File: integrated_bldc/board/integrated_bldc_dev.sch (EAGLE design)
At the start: 107 parts, among them J2 PRG

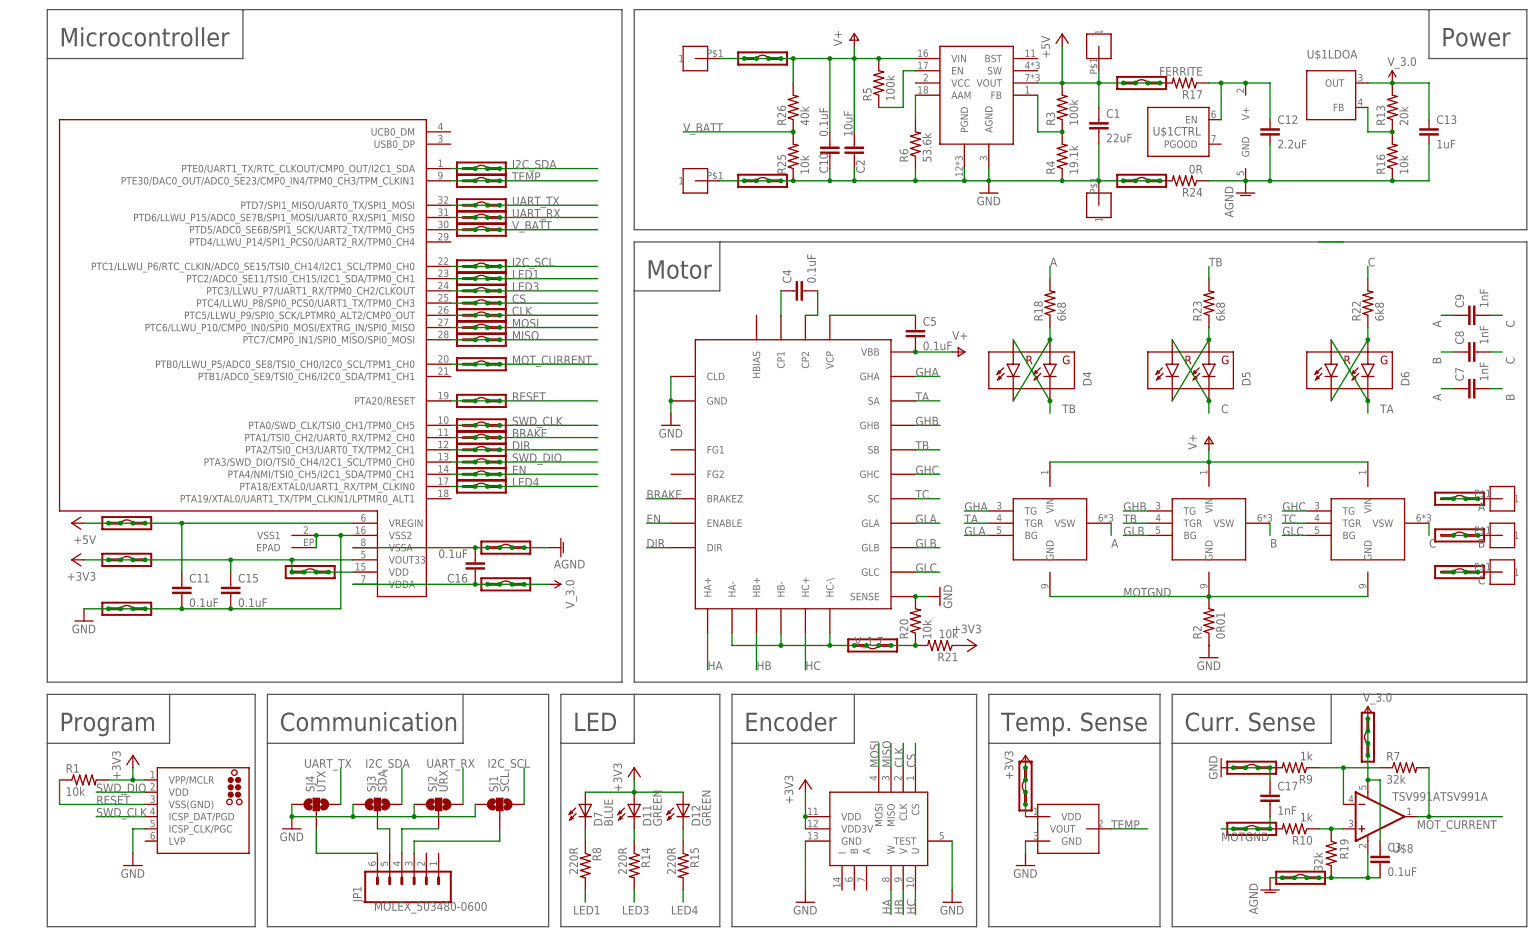
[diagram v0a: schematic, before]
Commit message: Finished Dev board layout. Added stop mask to vias. Corrected some component values based on part order.
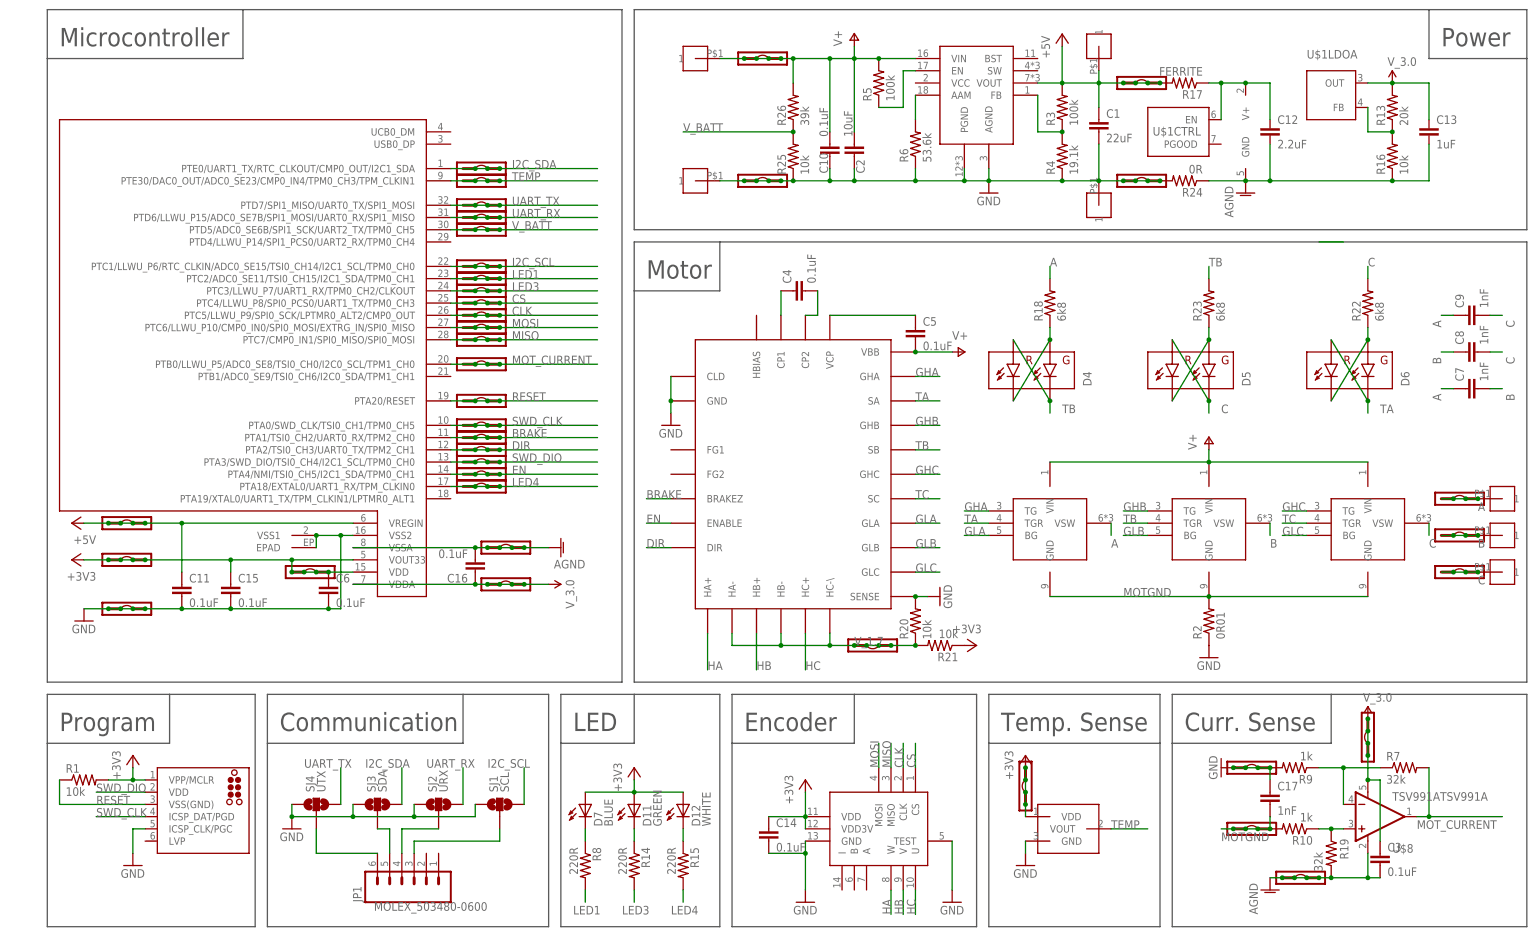
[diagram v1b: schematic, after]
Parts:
- added C14, C6: 0.1uF, SparkFun-Passives:CAP0402-CAP
- D12: value GREEN -> WHITE
- R26: value 40k -> 39k
- renumbered MOTA to A, MOTB to B, MOTC to C
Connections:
- net +3V3: now also C14.1, C6.1
- net GND: now also C14.2, C6.2
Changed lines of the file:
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@@
 <part name="D7" library="SparkFun-LED" deviceset="LED-BLUE" device="0603" value="BLUE"/>
 <part name="D11" library="SparkFun-LED" deviceset="LED-GREEN" device="0603" value="GREEN"/>
-<part name="D12" library="SparkFun-LED" deviceset="LED-GREEN" device="0603" value="GREEN"/>
+<part name="D12" library="SparkFun-LED" deviceset="LED-GREEN" device="0603" value="WHITE"/>
 <part name="R8" library="SparkFun-Passives" deviceset="RESISTOR" device="0402-RES" value="220R"/>
 <part name="R14" library="SparkFun-Passives" deviceset="RESISTOR" device="0402-RES" value="220R"/>
@@
 <part name="P+4" library="supply1" deviceset="V+" device=""/>
 <part name="R25" library="biomimetic" deviceset="RESISTOR" device="0402-RES" value="10k"/>
-<part name="R26" library="biomimetic" deviceset="RESISTOR" device="0402-RES" value="40k"/>
+<part name="R26" library="biomimetic" deviceset="RESISTOR" device="0402-RES" value="39k"/>
 <part name="P+5" library="supply1" deviceset="V+" device=""/>
 <part name="+3V4" library="supply1" deviceset="+3V3" device=""/>
@@
 <part name="V3.0" library="modular_robotics" deviceset="M04" device="LOCK"/>
 <part name="V1.7" library="modular_robotics" deviceset="M04" device="LOCK"/>
-<part name="MOTA" library="modular_robotics" deviceset="M04" device="LOCK"/>
-<part name="MOTB" library="modular_robotics" deviceset="M04" device="LOCK"/>
-<part name="MOTC" library="modular_robotics" deviceset="M04" device="LOCK"/>
+<part name="A" library="modular_robotics" deviceset="M04" device="LOCK"/>
+<part name="B" library="modular_robotics" deviceset="M04" device="LOCK"/>
+<part name="C" library="modular_robotics" deviceset="M04" device="LOCK"/>
+<part name="C6" library="SparkFun-Passives" deviceset="CAP" device="0402-CAP" value="0.1uF"/>
+<part name="C14" library="SparkFun-Passives" deviceset="CAP" device="0402-CAP" value="0.1uF"/>
 </parts>
 <sheets>
@@
 <instance part="V3.0" gate="G$1" x="208.28" y="119.38" rot="R180"/>
 <instance part="V1.7" gate="G$1" x="104.14" y="137.16" rot="R270"/>
-<instance part="MOTA" gate="G$1" x="228.6" y="167.64" rot="R90"/>
-<instance part="MOTB" gate="G$1" x="228.6" y="160.02" rot="R90"/>
-<instance part="MOTC" gate="G$1" x="228.6" y="152.4" rot="R90"/>
+<instance part="A" gate="G$1" x="228.6" y="167.64" rot="R90"/>
+<instance part="B" gate="G$1" x="228.6" y="160.02" rot="R90"/>
+<instance part="C" gate="G$1" x="228.6" y="152.4" rot="R90"/>
+<instance part="C6" gate="G$1" x="-7.62" y="147.32"/>
+<instance part="C14" gate="G$1" x="83.82" y="96.52"/>
 </instances>
 <busses>
@@
 <label x="231.14" y="165.1" size="1.778" layer="95"/>
 <pinref part="U$10" gate="G$1" pin="1"/>
-<pinref part="MOTA" gate="G$1" pin="1"/>
+<pinref part="A" gate="G$1" pin="1"/>
 <junction x="231.14" y="167.64"/>
-<pinref part="MOTA" gate="G$1" pin="2"/>
+<pinref part="A" gate="G$1" pin="2"/>
 <wire x1="228.6" y1="167.64" x2="226.06" y2="167.64" width="0.1524" layer="91"/>
 <junction x="228.6" y="167.64"/>
-<pinref part="MOTA" gate="G$1" pin="3"/>
+<pinref part="A" gate="G$1" pin="3"/>
 <wire x1="226.06" y1="167.64" x2="223.52" y2="167.64" width="0.1524" layer="91"/>
 <junction x="226.06" y="167.64"/>
-<pinref part="MOTA" gate="G$1" pin="4"/>
+<pinref part="A" gate="G$1" pin="4"/>
 </segment>
 <segment>
@@
 <label x="231.14" y="157.48" size="1.778" layer="95"/>
 <pinref part="U$11" gate="G$1" pin="1"/>
-<pinref part="MOTB" gate="G$1" pin="1"/>
+<pinref part="B" gate="G$1" pin="1"/>
 <junction x="231.14" y="160.02"/>
-<pinref part="MOTB" gate="G$1" pin="2"/>
+<pinref part="B" gate="G$1" pin="2"/>
 <wire x1="228.6" y1="160.02" x2="226.06" y2="160.02" width="0.1524" layer="91"/>
 <junction x="228.6" y="160.02"/>
-<pinref part="MOTB" gate="G$1" pin="3"/>
+<pinref part="B" gate="G$1" pin="3"/>
 <wire x1="226.06" y1="160.02" x2="223.52" y2="160.02" width="0.1524" layer="91"/>
 <junction x="226.06" y="160.02"/>
-<pinref part="MOTB" gate="G$1" pin="4"/>
+<pinref part="B" gate="G$1" pin="4"/>
 </segment>
 <segment>
@@
 <label x="231.14" y="149.86" size="1.778" layer="95"/>
 <pinref part="U$12" gate="G$1" pin="1"/>
-<pinref part="MOTC" gate="G$1" pin="1"/>
+<pinref part="C" gate="G$1" pin="1"/>
 <junction x="231.14" y="152.4"/>
-<pinref part="MOTC" gate="G$1" pin="2"/>
+<pinref part="C" gate="G$1" pin="2"/>
 <wire x1="228.6" y1="152.4" x2="226.06" y2="152.4" width="0.1524" layer="91"/>
 <junction x="228.6" y="152.4"/>
-<pinref part="MOTC" gate="G$1" pin="3"/>
+<pinref part="C" gate="G$1" pin="3"/>
 <wire x1="226.06" y1="152.4" x2="223.52" y2="152.4" width="0.1524" layer="91"/>
 <junction x="226.06" y="152.4"/>
-<pinref part="MOTC" gate="G$1" pin="4"/>
+<pinref part="C" gate="G$1" pin="4"/>
 </segment>
 <segment>
@@
 <pinref part="GND6" gate="1" pin="GND"/>
 <pinref part="AS5047P" gate="G$1" pin="GND"/>
-<wire x1="91.44" y1="86.36" x2="91.44" y2="96.52" width="0.1524" layer="91"/>
+<wire x1="91.44" y1="86.36" x2="91.44" y2="93.98" width="0.1524" layer="91"/>
+<pinref part="C14" gate="G$1" pin="2"/>
+<wire x1="91.44" y1="93.98" x2="91.44" y2="96.52" width="0.1524" layer="91"/>
+<wire x1="91.44" y1="93.98" x2="83.82" y2="93.98" width="0.1524" layer="91"/>
+<junction x="91.44" y="93.98"/>
 </segment>
 <segment>
@@
 <wire x1="-10.16" y1="157.48" x2="-10.16" y2="160.02" width="0.1524" layer="91"/>
 <junction x="-10.16" y="160.02"/>
-<wire x1="-27.94" y1="144.78" x2="-5.08" y2="144.78" width="0.1524" layer="91"/>
+<wire x1="-27.94" y1="144.78" x2="-7.62" y2="144.78" width="0.1524" layer="91"/>
+<wire x1="-7.62" y1="144.78" x2="-5.08" y2="144.78" width="0.1524" layer="91"/>
 <wire x1="-5.08" y1="144.78" x2="-5.08" y2="160.02" width="0.1524" layer="91"/>
 <junction x="-27.94" y="144.78"/>
@@
 <junction x="-50.8" y="144.78"/>
 <junction x="-48.26" y="144.78"/>
+<pinref part="C6" gate="G$1" pin="2"/>
+<junction x="-7.62" y="144.78"/>
 </segment>
 </net>
@@
 <junction x="91.44" y="101.6"/>
 <pinref part="+3V4" gate="G$1" pin="+3V3"/>
+<pinref part="C14" gate="G$1" pin="1"/>
+<wire x1="91.44" y1="101.6" x2="83.82" y2="101.6" width="0.1524" layer="91"/>
 </segment>
 <segment>
@@
 <junction x="-12.7" y="152.4"/>
 <junction x="-10.16" y="152.4"/>
-</segment>
-</net>
+<pinref part="C6" gate="G$1" pin="1"/>
+</segment>
+</net>
